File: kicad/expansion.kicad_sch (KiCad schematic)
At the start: 23 parts, among them J10 PJ-063AH, J11 Conn_02x01, J4 ESW-106-44-T-S, J5 PH2-06-UA, J6 ESW-112-44-T-S, J7 Conn_01x10, J8 ESW-112-44-T-S, J9 Conn_01x10, SW1 PTS810 SJM 250 SMTR LFS, SW2 PTS810 SJM 250 SMTR LFS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

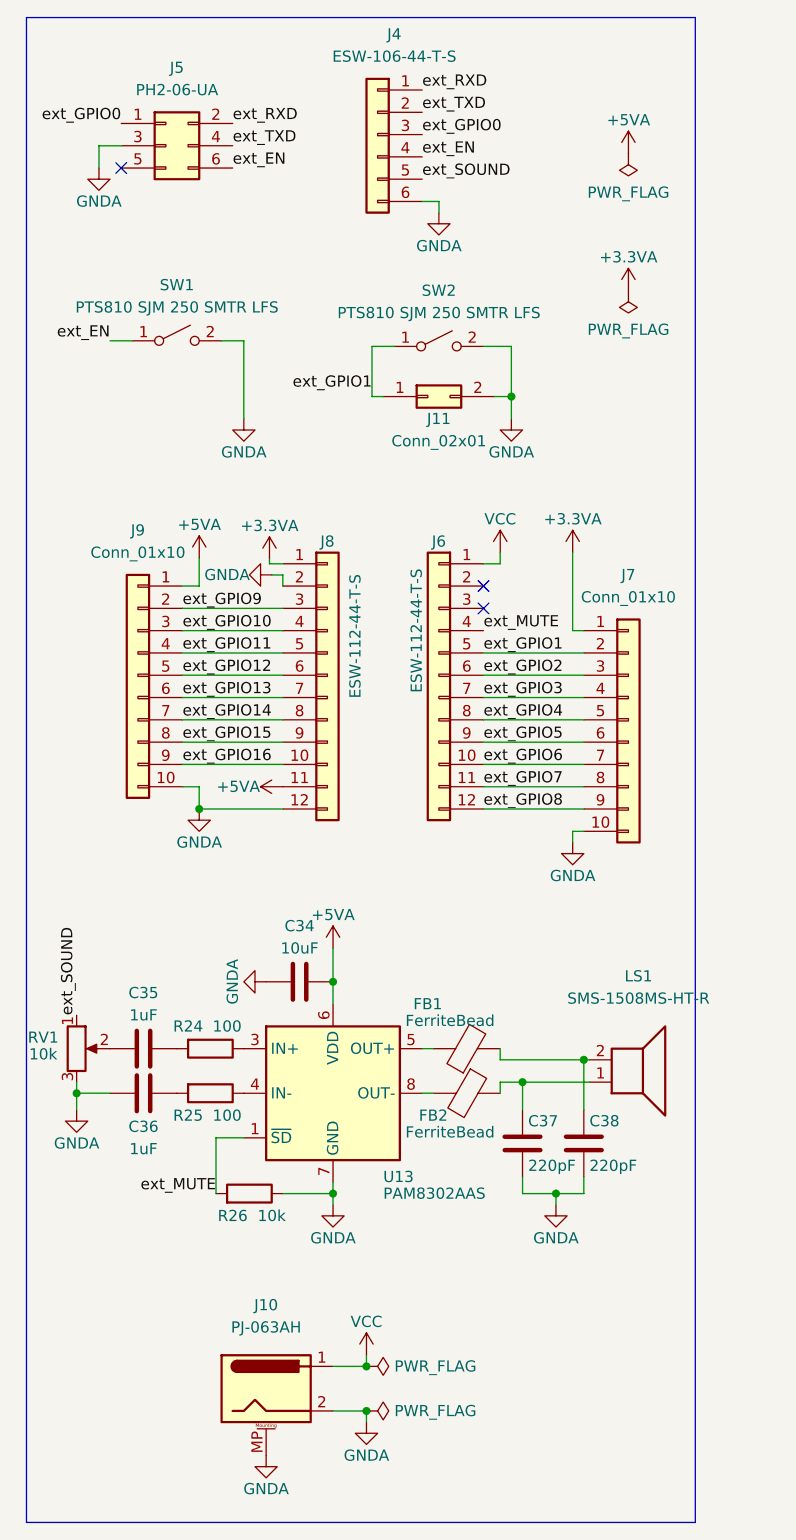
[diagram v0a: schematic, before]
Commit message: Cleaned up speaker footprint, some routing, and some caps
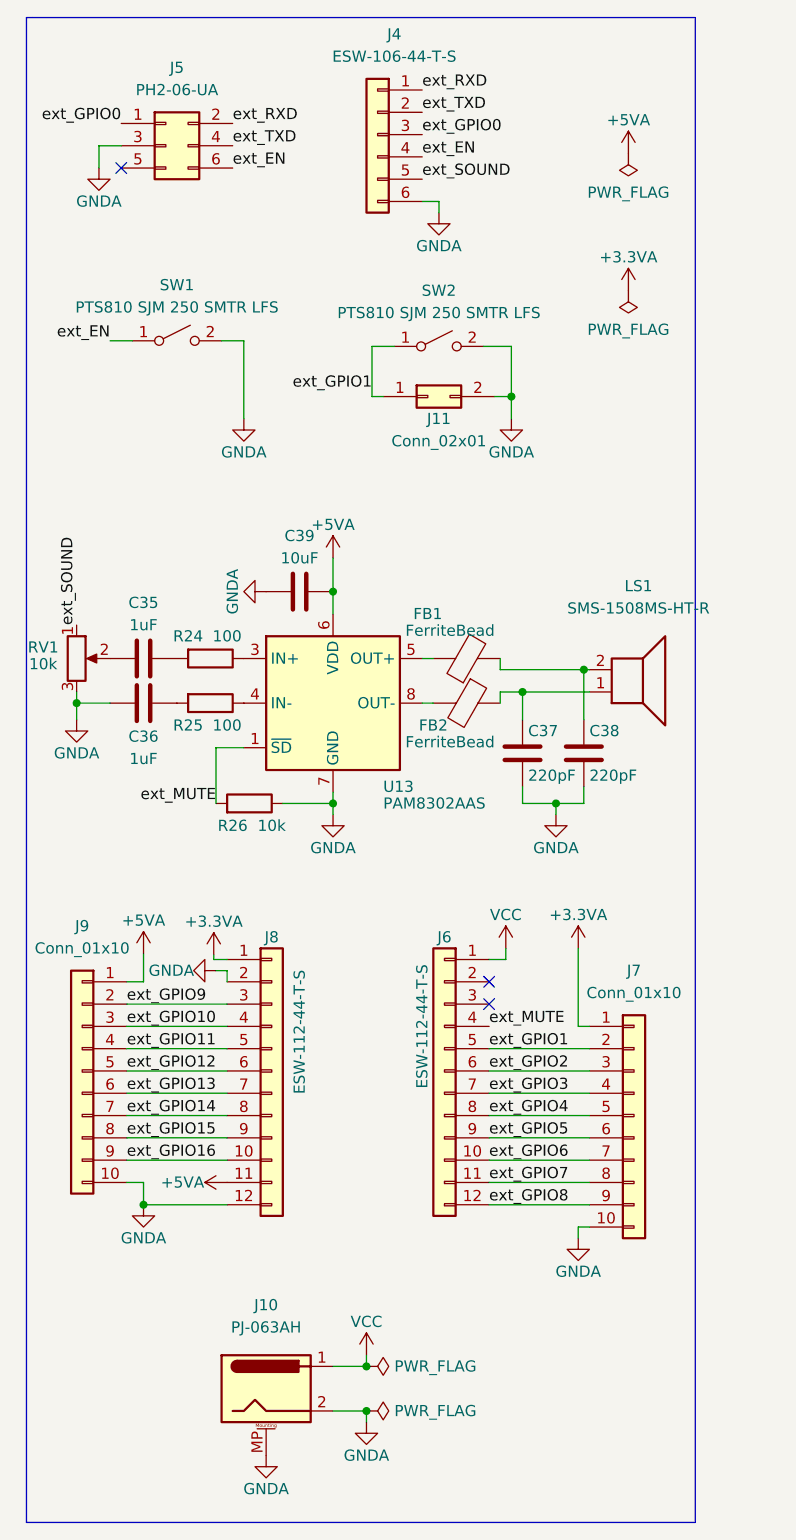
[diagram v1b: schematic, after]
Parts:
- renumbered C34 to C39
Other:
- moved on the sheet: C35, C36, C37, C38, C39, FB1, FB2, J6, J7, J8, J9, LS1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

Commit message: Lowered amp's pulldown resistor from 10k to 1k
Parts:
- added C40: 10uF, Capacitor_Tantalum_SMD:CP_EIA-3216-10_Kemet-I, symbol Device:C_Polarized
- C39: value 10uF -> 1uF
- R26: value 10k -> 1k
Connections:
- net +5VA: now also C40.1
- net GNDA: now also C40.2
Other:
- moved on the sheet: C39
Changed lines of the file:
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@@
 (kicad_sch (version 20211123) (generator eeschema)
   (paper "A4")
+  (junction (at 139.7 107.95) (diameter 0) (color 0 0 0 0)
+  )
+  (junction (at 118.11 172.085) (diameter 0) (color 0 0 0 0)
+  )
+  (junction (at 135.89 95.25) (diameter 0) (color 0 0 0 0)
+  )
+  (junction (at 118.11 177.165) (diameter 0) (color 0 0 0 0)
+  )
+  (junction (at 142.875 92.71) (diameter 0) (color 0 0 0 0)
+  )
+  (junction (at 114.3 77.47) (diameter 0) (color 0 0 0 0)
+  )
+  (junction (at 102.87 83.82) (diameter 0) (color 0 0 0 0)
+  )
+  (junction (at 114.3 107.95) (diameter 0) (color 0 0 0 0)
+  )
+  (junction (at 134.62 61.595) (diameter 0) (color 0 0 0 0)
+  )
+  (junction (at 92.71 153.67) (diameter 0) (color 0 0 0 0)
+  )
   (junction (at 114.3 83.82) (diameter 0) (color 0 0 0 0)
-  )
-  (junction (at 139.7 107.95) (diameter 0) (color 0 0 0 0)
-  )
-  (junction (at 118.11 172.085) (diameter 0) (color 0 0 0 0)
-  )
-  (junction (at 135.89 95.25) (diameter 0) (color 0 0 0 0)
-  )
-  (junction (at 118.11 177.165) (diameter 0) (color 0 0 0 0)
-  )
-  (junction (at 142.875 92.71) (diameter 0) (color 0 0 0 0)
-  )
-  (junction (at 114.3 107.95) (diameter 0) (color 0 0 0 0)
-  )
-  (junction (at 134.62 61.595) (diameter 0) (color 0 0 0 0)
-  )
-  (junction (at 92.71 153.67) (diameter 0) (color 0 0 0 0)
   )
   (junction (at 85.09 96.52) (diameter 0) (color 0 0 0 0)
@@
     (stroke (width 0) (type default) (color 0 0 0 0))
   )
+  (wire (pts (xy 102.235 83.82) (xy 102.87 83.82))
+    (stroke (width 0) (type default) (color 0 0 0 0))
+  )
   (wire (pts (xy 133.35 95.25) (xy 133.35 96.52))
     (stroke (width 0) (type default) (color 0 0 0 0))
@@
     (stroke (width 0) (type default) (color 0 0 0 0))
   )
+  (wire (pts (xy 102.87 77.47) (xy 104.775 77.47))
+    (stroke (width 0) (type default) (color 0 0 0 0))
+  )
   (wire (pts (xy 102.235 146.05) (xy 90.805 146.05))
     (stroke (width 0) (type default) (color 0 0 0 0))
@@
     (stroke (width 0) (type default) (color 0 0 0 0))
   )
+  (wire (pts (xy 114.3 83.82) (xy 114.3 86.36))
+    (stroke (width 0) (type default) (color 0 0 0 0))
+  )
   (wire (pts (xy 102.235 138.43) (xy 90.805 138.43))
     (stroke (width 0) (type default) (color 0 0 0 0))
@@
     (stroke (width 0) (type default) (color 0 0 0 0))
   )
-  (wire (pts (xy 114.3 80.01) (xy 114.3 83.82))
-    (stroke (width 0) (type default) (color 0 0 0 0))
-  )
   (wire (pts (xy 132.715 61.595) (xy 134.62 61.595))
     (stroke (width 0) (type default) (color 0 0 0 0))
@@
     (stroke (width 0) (type default) (color 0 0 0 0))
   )
-  (wire (pts (xy 114.3 83.82) (xy 114.3 86.36))
+  (wire (pts (xy 114.3 72.39) (xy 114.3 77.47))
     (stroke (width 0) (type default) (color 0 0 0 0))
   )
@@
     (stroke (width 0) (type default) (color 0 0 0 0))
   )
+  (wire (pts (xy 102.87 83.82) (xy 104.775 83.82))
+    (stroke (width 0) (type default) (color 0 0 0 0))
+  )
   (wire (pts (xy 132.08 125.73) (xy 133.985 125.73))
     (stroke (width 0) (type default) (color 0 0 0 0))
@@
     (stroke (width 0) (type default) (color 0 0 0 0))
   )
+  (wire (pts (xy 102.87 83.82) (xy 102.87 77.47))
+    (stroke (width 0) (type default) (color 0 0 0 0))
+  )
   (wire (pts (xy 143.51 151.13) (xy 132.08 151.13))
     (stroke (width 0) (type default) (color 0 0 0 0))
@@
     (stroke (width 0) (type default) (color 0 0 0 0))
   )
+  (wire (pts (xy 114.3 77.47) (xy 114.3 83.82))
+    (stroke (width 0) (type default) (color 0 0 0 0))
+  )
   (wire (pts (xy 102.235 125.73) (xy 100.711 125.73))
     (stroke (width 0) (type default) (color 0 0 0 0))
@@
     (stroke (width 0) (type default) (color 0 0 0 0))
   )
+  (wire (pts (xy 112.395 83.82) (xy 114.3 83.82))
+    (stroke (width 0) (type default) (color 0 0 0 0))
+  )
   (wire (pts (xy 134.62 55.88) (xy 131.445 55.88))
     (stroke (width 0) (type default) (color 0 0 0 0))
@@
   )
   (wire (pts (xy 102.235 127) (xy 102.235 128.27))
+    (stroke (width 0) (type default) (color 0 0 0 0))
+  )
+  (wire (pts (xy 112.395 77.47) (xy 114.3 77.47))
     (stroke (width 0) (type default) (color 0 0 0 0))
   )
@@
     (pin "1")
   )
-  (symbol (lib_id "power:+5VA") (at 114.3 80.01 0) (unit 1)
-    (in_bom yes) (on_board yes)
-    (property "Reference" "#PWR032" (id 0) (at 114.3 83.82 0)
-      (effects (font (size 1.27 1.27)) hide)
-    )
-    (property "Value" "+5VA" (id 1) (at 114.3 76.2 0))
-    (property "Footprint" "" (id 2) (at 114.3 80.01 0)
-      (effects (font (size 1.27 1.27)) hide)
-    )
-    (property "Datasheet" "" (id 3) (at 114.3 80.01 0)
-      (effects (font (size 1.27 1.27)) hide)
-    )
-    (pin "1")
+  (symbol (lib_id "power:+5VA") (at 114.3 72.39 0) (unit 1)
+    (in_bom yes) (on_board yes)
+    (property "Reference" "#PWR032" (id 0) (at 114.3 76.2 0)
+      (effects (font (size 1.27 1.27)) hide)
+    )
+    (property "Value" "+5VA" (id 1) (at 114.3 68.58 0))
+    (property "Footprint" "" (id 2) (at 114.3 72.39 0)
+      (effects (font (size 1.27 1.27)) hide)
+    )
+    (property "Datasheet" "" (id 3) (at 114.3 72.39 0)
+      (effects (font (size 1.27 1.27)) hide)
+    )
+    (pin "1")
+  )
+  (symbol (lib_id "Device:C_Polarized") (at 108.585 77.47 270) (mirror x) (unit 1)
+    (in_bom yes) (on_board yes)
+    (property "Reference" "C40" (id 0) (at 105.41 75.565 90))
+    (property "Value" "10uF" (id 1) (at 112.395 75.565 90))
+    (property "Footprint" "Capacitor_Tantalum_SMD:CP_EIA-3216-10_Kemet-I" (id 2) (at 104.775 76.5048 0)
+      (effects (font (size 1.27 1.27)) hide)
+    )
+    (property "Datasheet" "~" (id 3) (at 108.585 77.47 0)
+      (effects (font (size 1.27 1.27)) hide)
+    )
+    (pin "1")
+    (pin "2")
   )
   (symbol (lib_id "power:+3.3VA") (at 147.955 49.53 0) (unit 1)
@@
     (pin "6")
   )
-  (symbol (lib_id "power:GNDA") (at 106.68 83.82 270) (unit 1)
-    (in_bom yes) (on_board yes)
-    (property "Reference" "#PWR033" (id 0) (at 100.33 83.82 0)
-      (effects (font (size 1.27 1.27)) hide)
-    )
-    (property "Value" "GNDA" (id 1) (at 102.87 83.82 0))
-    (property "Footprint" "" (id 2) (at 106.68 83.82 0)
-      (effects (font (size 1.27 1.27)) hide)
-    )
-    (property "Datasheet" "" (id 3) (at 106.68 83.82 0)
+  (symbol (lib_id "power:GNDA") (at 102.235 83.82 270) (unit 1)
+    (in_bom yes) (on_board yes)
+    (property "Reference" "#PWR033" (id 0) (at 95.885 83.82 0)
+      (effects (font (size 1.27 1.27)) hide)
+    )
+    (property "Value" "GNDA" (id 1) (at 98.425 83.82 0))
+    (property "Footprint" "" (id 2) (at 102.235 83.82 0)
+      (effects (font (size 1.27 1.27)) hide)
+    )
+    (property "Datasheet" "" (id 3) (at 102.235 83.82 0)
       (effects (font (size 1.27 1.27)) hide)
     )
@@
     (pin "1")
   )
-  (symbol (lib_id "Device:C") (at 110.49 83.82 270) (unit 1)
-    (in_bom yes) (on_board yes)
-    (property "Reference" "C39" (id 0) (at 110.49 77.47 90))
-    (property "Value" "10uF" (id 1) (at 110.49 80.01 90))
-    (property "Footprint" "Capacitor_SMD:C_0805_2012Metric" (id 2) (at 106.68 84.7852 0)
-      (effects (font (size 1.27 1.27)) hide)
-    )
-    (property "Datasheet" "~" (id 3) (at 110.49 83.82 0)
+  (symbol (lib_id "Device:C") (at 108.585 83.82 270) (unit 1)
+    (in_bom yes) (on_board yes)
+    (property "Reference" "C39" (id 0) (at 105.41 81.28 90))
+    (property "Value" "1uF" (id 1) (at 111.76 81.28 90))
+    (property "Footprint" "Capacitor_SMD:C_0805_2012Metric" (id 2) (at 104.775 84.7852 0)
+      (effects (font (size 1.27 1.27)) hide)
+    )
+    (property "Datasheet" "~" (id 3) (at 108.585 83.82 0)
       (effects (font (size 1.27 1.27)) hide)
     )
@@
     (in_bom yes) (on_board yes)
     (property "Reference" "R26" (id 0) (at 102.87 110.49 90))
-    (property "Value" "10k" (id 1) (at 107.315 110.49 90))
+    (property "Value" "1k" (id 1) (at 107.315 110.49 90))
     (property "Footprint" "Resistor_SMD:R_0805_2012Metric" (id 2) (at 104.775 109.728 90)
       (effects (font (size 1.27 1.27)) hide)

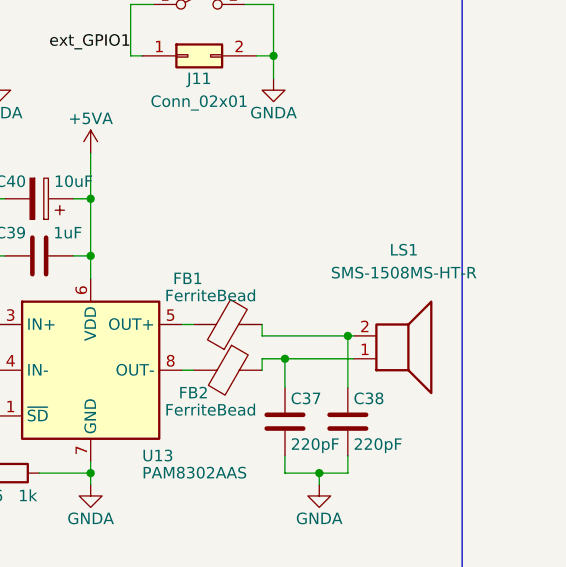
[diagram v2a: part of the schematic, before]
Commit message: Adjust component placement around U13
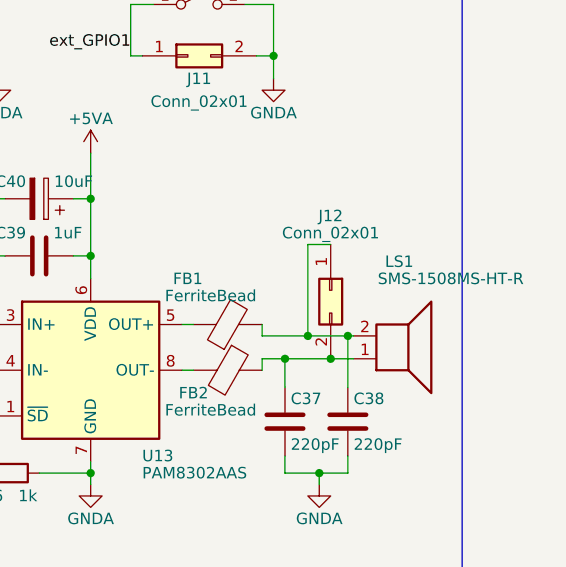
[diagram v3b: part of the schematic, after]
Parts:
- added J12: Conn_02x01, Connector_PinHeader_2.54mm:PinHeader_1x02_P2.54mm_Vertical, symbol Connector_Generic:Conn_02x01
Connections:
- net at C38.1, FB1.2, LS1.2: now also J12.1 (Pin_1)
- net at C37.1, FB2.1, LS1.1: now also J12.2 (Pin_2)
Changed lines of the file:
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@@
   (junction (at 135.89 95.25) (diameter 0) (color 0 0 0 0)
   )
+  (junction (at 138.43 92.71) (diameter 0) (color 0 0 0 0)
+  )
   (junction (at 118.11 177.165) (diameter 0) (color 0 0 0 0)
   )
@@
   )
   (junction (at 114.3 77.47) (diameter 0) (color 0 0 0 0)
+  )
+  (junction (at 140.97 95.25) (diameter 0) (color 0 0 0 0)
   )
   (junction (at 102.87 83.82) (diameter 0) (color 0 0 0 0)
@@
     (stroke (width 0) (type default) (color 0 0 0 0))
   )
+  (wire (pts (xy 138.43 92.71) (xy 142.875 92.71))
+    (stroke (width 0) (type default) (color 0 0 0 0))
+  )
   (wire (pts (xy 92.71 128.27) (xy 90.805 128.27))
     (stroke (width 0) (type default) (color 0 0 0 0))
@@
     (stroke (width 0) (type default) (color 0 0 0 0))
   )
+  (wire (pts (xy 140.97 95.25) (xy 143.51 95.25))
+    (stroke (width 0) (type default) (color 0 0 0 0))
+  )
   (wire (pts (xy 143.51 140.97) (xy 132.08 140.97))
     (stroke (width 0) (type default) (color 0 0 0 0))
@@
     (stroke (width 0) (type default) (color 0 0 0 0))
   )
-  (wire (pts (xy 135.89 95.25) (xy 143.51 95.25))
+  (wire (pts (xy 135.89 95.25) (xy 140.97 95.25))
     (stroke (width 0) (type default) (color 0 0 0 0))
   )
@@
     (stroke (width 0) (type default) (color 0 0 0 0))
   )
+  (wire (pts (xy 140.97 82.55) (xy 138.43 82.55))
+    (stroke (width 0) (type default) (color 0 0 0 0))
+  )
   (wire (pts (xy 102.235 125.73) (xy 100.711 125.73))
     (stroke (width 0) (type default) (color 0 0 0 0))
@@
     (stroke (width 0) (type default) (color 0 0 0 0))
   )
+  (wire (pts (xy 138.43 82.55) (xy 138.43 92.71))
+    (stroke (width 0) (type default) (color 0 0 0 0))
+  )
   (wire (pts (xy 118.745 55.88) (xy 121.285 55.88))
     (stroke (width 0) (type default) (color 0 0 0 0))
@@
     (stroke (width 0) (type default) (color 0 0 0 0))
   )
-  (wire (pts (xy 133.35 92.71) (xy 142.875 92.71))
+  (wire (pts (xy 133.35 92.71) (xy 138.43 92.71))
     (stroke (width 0) (type default) (color 0 0 0 0))
   )
@@
     )
     (property "Datasheet" "~" (id 3) (at 108.585 77.47 0)
+      (effects (font (size 1.27 1.27)) hide)
+    )
+    (pin "1")
+    (pin "2")
+  )
+  (symbol (lib_id "Connector_Generic:Conn_02x01") (at 140.97 87.63 270) (unit 1)
+    (in_bom yes) (on_board yes)
+    (property "Reference" "J12" (id 0) (at 140.97 79.375 90))
+    (property "Value" "Conn_02x01" (id 1) (at 140.97 81.28 90))
+    (property "Footprint" "Connector_PinHeader_2.54mm:PinHeader_1x02_P2.54mm_Vertical" (id 2) (at 140.97 87.63 0)
+      (effects (font (size 1.27 1.27)) hide)
+    )
+    (property "Datasheet" "~" (id 3) (at 140.97 87.63 0)
       (effects (font (size 1.27 1.27)) hide)
     )
@@
   )
   (symbol (lib_id "starman:SMS-1508MS-HT-R") (at 148.59 95.25 0) (mirror x) (unit 1)
-    (in_bom yes) (on_board yes) (fields_autoplaced)
-    (property "Reference" "LS1" (id 0) (at 149.098 83.185 0))
-    (property "Value" "SMS-1508MS-HT-R" (id 1) (at 149.098 85.725 0))
+    (in_bom yes) (on_board yes)
+    (property "Reference" "LS1" (id 0) (at 148.59 84.455 0))
+    (property "Value" "SMS-1508MS-HT-R" (id 1) (at 154.305 86.36 0))
     (property "Footprint" "starman:SPKR_SMS-1508MS-HT-R" (id 2) (at 148.59 90.17 0)
       (effects (font (size 1.27 1.27)) hide)
